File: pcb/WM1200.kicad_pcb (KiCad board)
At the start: 4 copper layers, 159 x 104 mm, 143 parts, among them Q1 BC817, Q2 BC817, Q3 BC817, Q4 BC817, Q5 BC817, Q6 BC817, U1 74LVCH162245A, U2 74LVCH162245A, U3 74LVCH162245A, U4 74LVCH162245A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

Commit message: ready for production
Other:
- board size 159 x 104 mm -> 147 x 104 mm
- board text removed: "TODO: replace all microvias with ordinary (yet small) vias"
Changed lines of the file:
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@@
   (general
     (thickness 1.6)
-    (drawings 12)
+    (drawings 11)
     (tracks 11043)
     (zones 0)
@@
     (solder_mask_min_width 0.25)
     (aux_axis_origin 0 0)
-    (grid_origin 90 150)
+    (grid_origin 101.9 150)
     (visible_elements 7FFFFFFF)
     (pcbplotparams
@@
   (module WM1200:ac7020 (layer F.Cu)
     (at 137.9 142.6)
-    (fp_text reference X3 (at 35.5253 -32.1868) (layer F.SilkS)
+    (fp_text reference X3 (at 69.85 -5.5) (layer F.SilkS)
       (effects (font (size 1 1) (thickness 0.15)))
     )
@@
   (module WM1200:Trapdoor_connector locked (layer F.Cu)
     (at 109.5 146.25)
-    (fp_text reference X2 (at 2.35 2.7) (layer F.SilkS)
+    (fp_text reference X2 (at -5.95 -32) (layer F.SilkS)
       (effects (font (size 1 1) (thickness 0.15)))
     )
@@
       (effects (font (size 1 1) (thickness 0.15)))
     )
+    (fp_line (start -6.985 3.175) (end -19.05 3.175) (layer Dwgs.User) (width 0.12))
+    (fp_line (start -19.05 -99.695) (end -6.985 -99.695) (layer Dwgs.User) (width 0.12))
     (fp_text user 2 (at -3.81 1.905) (layer F.SilkS)
       (effects (font (size 1 1) (thickness 0.15)))
@@
     )
     (fp_line (start -6.985 -99.695) (end -6.985 3.175) (layer B.SilkS) (width 0.12))
-    (fp_line (start 1.27 -99.695) (end -19.05 -99.695) (layer B.SilkS) (width 0.12))
-    (fp_line (start -19.05 3.175) (end 1.27 3.175) (layer B.SilkS) (width 0.12))
-    (fp_line (start -19.05 3.175) (end -19.05 -99.695) (layer B.SilkS) (width 0.12))
+    (fp_line (start 1.27 -99.695) (end -6.985 -99.695) (layer B.SilkS) (width 0.12))
+    (fp_line (start -6.985 3.175) (end 1.27 3.175) (layer B.SilkS) (width 0.12))
+    (fp_line (start -19.05 3.175) (end -19.05 -99.695) (layer Dwgs.User) (width 0.12))
     (fp_line (start 1.27 3.175) (end 1.27 -99.695) (layer B.SilkS) (width 0.12))
     (fp_text user 1 (at 0 1.905) (layer F.SilkS)
@@
     )
   )
-  (gr_text "TODO:\nreplace all microvias with ordinary (yet small) vias" (at 128.1 161.1) (layer Dwgs.User)
-    (effects (font (size 1.5 1.5) (thickness 0.3)))
-  )
   (gr_text "In me the Wishmaster" (at 230.5 106.8) (layer In2.Cu)
     (effects (font (size 1.5 1.5) (thickness 0.3)))
@@
   )
   (gr_text "Wishmaster 1200" (at 230.5 93.2) (layer F.SilkS)
-    (effects (font (size 2 2) (thickness 0.15) italic))
+    (effects (font (size 2 2) (thickness 0.4) italic))
   )
-  (gr_line (start 249 150) (end 90 150) (layer Edge.Cuts) (width 0.05))
-  (gr_line (start 249 74) (end 249 150) (layer Edge.Cuts) (width 0.05))
-  (gr_line (start 151 74) (end 249 74) (layer Edge.Cuts) (width 0.05))
+  (gr_line (start 248.9 150) (end 101.9 150) (layer Edge.Cuts) (width 0.05))
+  (gr_line (start 248.9 74) (end 248.9 150) (layer Edge.Cuts) (width 0.05))
+  (gr_line (start 151 74) (end 248.9 74) (layer Edge.Cuts) (width 0.05))
   (gr_line (start 151 46) (end 151 74) (layer Edge.Cuts) (width 0.05))
-  (gr_line (start 90 46) (end 151 46) (layer Edge.Cuts) (width 0.05))
-  (gr_line (start 90 150) (end 90 46) (layer Edge.Cuts) (width 0.05))
+  (gr_line (start 101.9 46) (end 151 46) (layer Edge.Cuts) (width 0.05))
+  (gr_line (start 101.9 150) (end 101.9 46) (layer Edge.Cuts) (width 0.05))
   (via (at 134.425 99.62) (size 0.6) (drill 0.3) (layers F.Cu B.Cu) (net 1))
   (via (at 123.475 95.925) (size 0.6) (drill 0.3) (layers F.Cu B.Cu) (net 1))
@@
     (polygon
       (pts
-        (xy 151 74) (xy 249 74) (xy 249 150) (xy 90 150) (xy 90 46)
+        (xy 151 74) (xy 248.9 74) (xy 248.9 150) (xy 101.9 150) (xy 101.9 46)
         (xy 151 46)
       )
@@
     (polygon
       (pts
-        (xy 120 150) (xy 90 150) (xy 90 46) (xy 120 46)
+        (xy 120 150) (xy 101.9 150) (xy 101.9 46) (xy 120 46)
       )
     )
@@
     (polygon
       (pts
-        (xy 151 74) (xy 249 74) (xy 249 150) (xy 138.4 150) (xy 138.4 46)
+        (xy 151 74) (xy 248.9 74) (xy 248.9 150) (xy 138.4 150) (xy 138.4 46)
         (xy 151 46)
       )

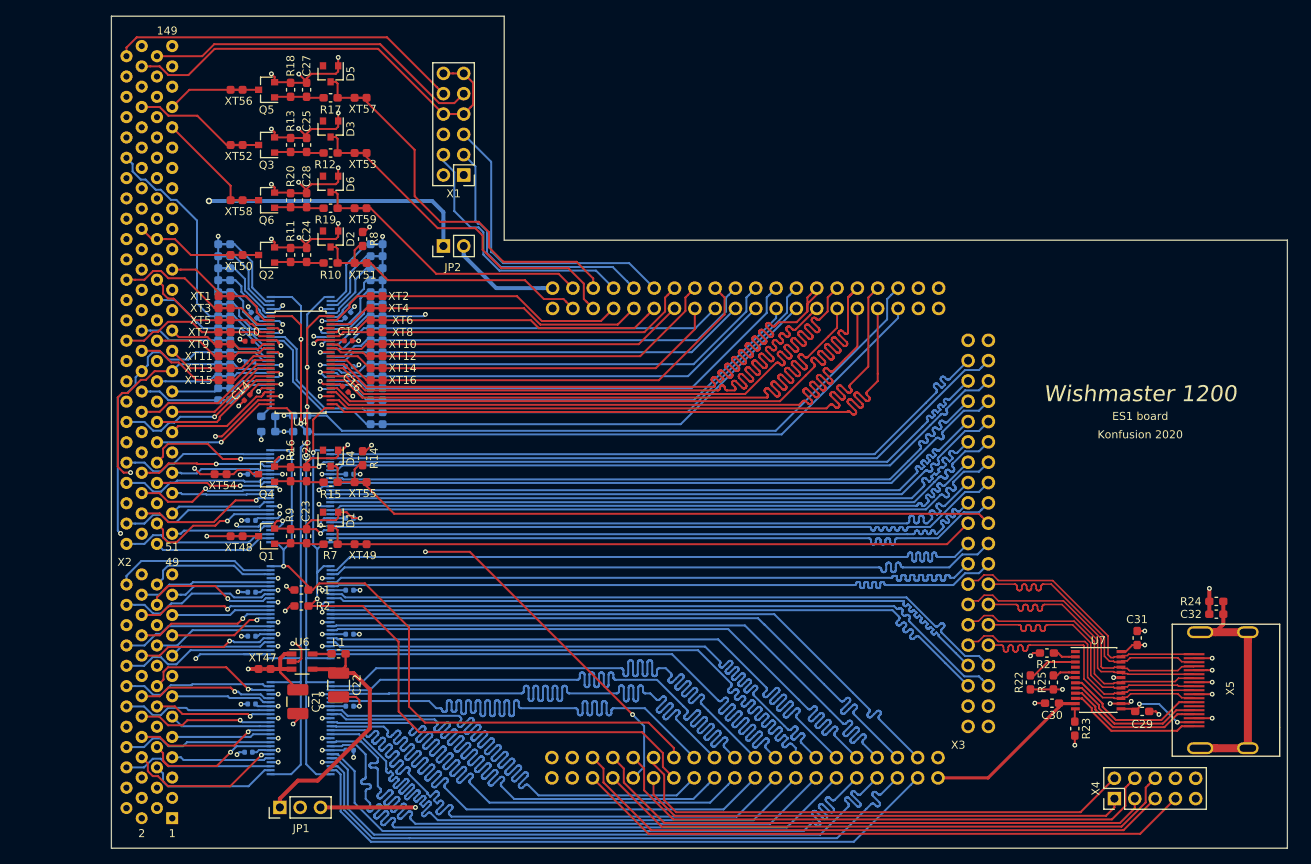
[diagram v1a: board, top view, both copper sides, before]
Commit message: board updated - factory DRC checking in progress
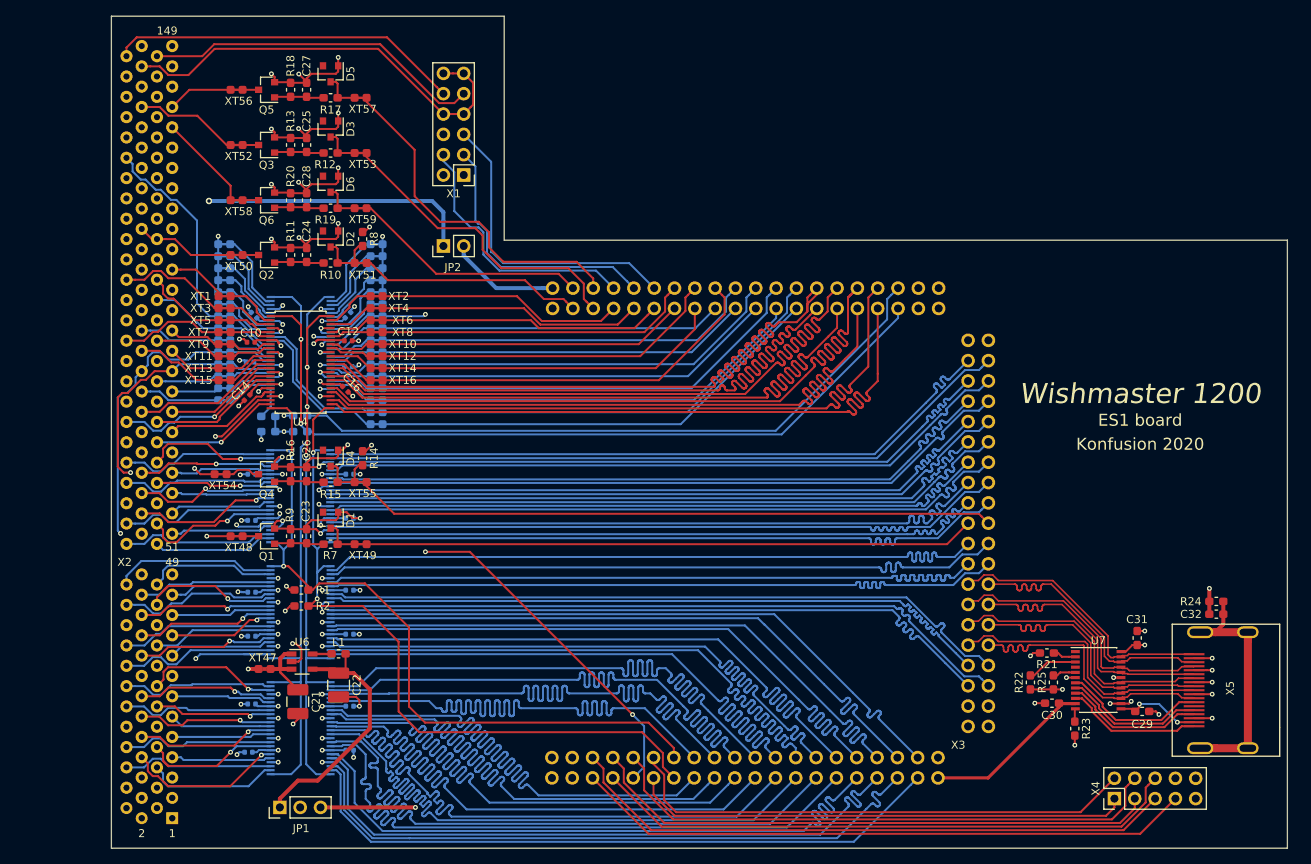
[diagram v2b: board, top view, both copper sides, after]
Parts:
- JP1: footprint Connector_PinHeader_2.54mm:PinHeader_1x03_P2.54mm_Vertical -> WM1200:PinHeader_1x03_P2.54mm_Vertical
- JP2: footprint Connector_PinHeader_2.54mm:PinHeader_1x02_P2.54mm_Vertical -> WM1200:PinHeader_1x02_P2.54mm_Vertical
- X1: footprint Connector_PinHeader_2.54mm:PinHeader_2x06_P2.54mm_Vertical -> WM1200:PinHeader_2x06_P2.54mm_Vertical
- X4: footprint Connector_PinHeader_2.54mm:PinHeader_2x05_P2.54mm_Vertical -> WM1200:PinHeader_2x05_P2.54mm_Vertical
- moved C10 0.26 mm to (119.3, 86.8)
- moved C19 0.12 mm to (131.5, 89.8)
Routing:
- net +3V3_DC_DC: track 32.7 -> 31.4 mm

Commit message: factory DRC passed
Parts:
- D1, D2, D3, D4, D5, D6: footprint Diode_SMD:D_SOT-23_ANK -> WM1200:D_SOT-23_ANK
- Q1, Q2, Q3, Q4, Q5, Q6: footprint Package_TO_SOT_SMD:SOT-23 -> WM1200:SOT-23
- U6: footprint Package_TO_SOT_SMD:TSOT-23-5 -> WM1200:TSOT-23-5
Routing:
- net GND: track 209.9 -> 210.8 mm
